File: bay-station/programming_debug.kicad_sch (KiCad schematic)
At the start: 11 parts, among them J3 USB_C_Receptacle_USB2.0_14P, SW1 BOOT, SW2 RESET

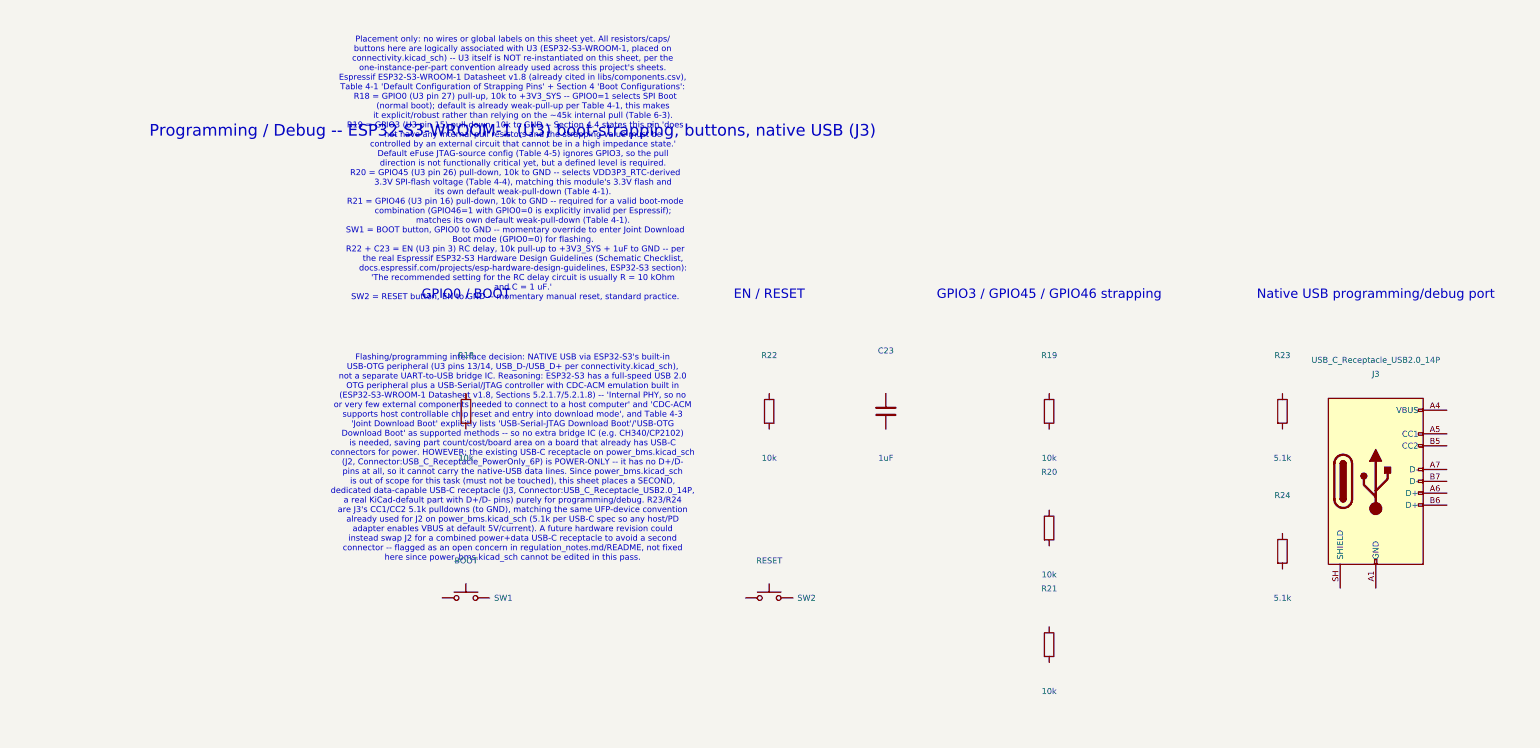
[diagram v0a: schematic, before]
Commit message: Bay station: discrete DW3210 array on a shared clock, Nordic BT840 host
Two coupled changes, both forced by the positioning scheme.

UWB ARRAY. TDoA compares timestamps across receivers, so they must share a
time base. The DWM3000 module makes that impossible -- its 24 pins contain
no clock pin and its crystal is internal and unreachable, so four of them
cannot be synchronised at any price. The bare DW3000 IC can: Datasheet v1.3
Table 10 states a 38.4 MHz signal may be supplied from an external reference
via the XTI overdrive pin. Four DW3210s (QFN40, not the 52-ball WLCSP
DW3110 the module is built on) now sit on one PCB sharing one TCXO through
a 1:4 low-skew buffer, with the antennas remote on ~1-2 m SMA coax. This
makes synchronisation structurally absent rather than solved.

uwb_anchors.kicad_sch renamed to uwb_array.kicad_sch -- the four receivers
are one on-board array, not distributed anchor units. U4 is A0, the CENTER
anchor; U5-U7 are A1-A3 outer. They are not interchangeable peers.

New clock_dist.kicad_sch holds the shared reference network. Placed are only
the passives the datasheet actually specifies: 2200 pF AC coupling into each
XTI and 1 pF from each XTO to ground, both required only because an external
clock is used. TCXO and buffer parts are not yet selected.

HOST MCU. The uplink moved from WiFi-to-internet to BLE-to-a-laptop, and
WiFi was the only thing keeping this board off Nordic. ESP32-S3-WROOM-1 is
replaced by a Fanstel BT840 (nRF52840), which gives one toolchain across
both boards and aligns with Qorvo's DW3000 reference stack -- easing the
multi-instance driver work that sits on the critical path. Note the
ESP32-S3 is BLE-only with no Classic/SPP, so the laptop link is a GATT
service.

programming_debug collapsed accordingly: Nordic programs over SWD, so the
boot straps, EN RC delay, BOOT button and the data-capable USB-C are gone,
replaced by a 2x5 ARM Cortex Debug header. That RESOLVES the long-standing
two-USB-C open item by deletion -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
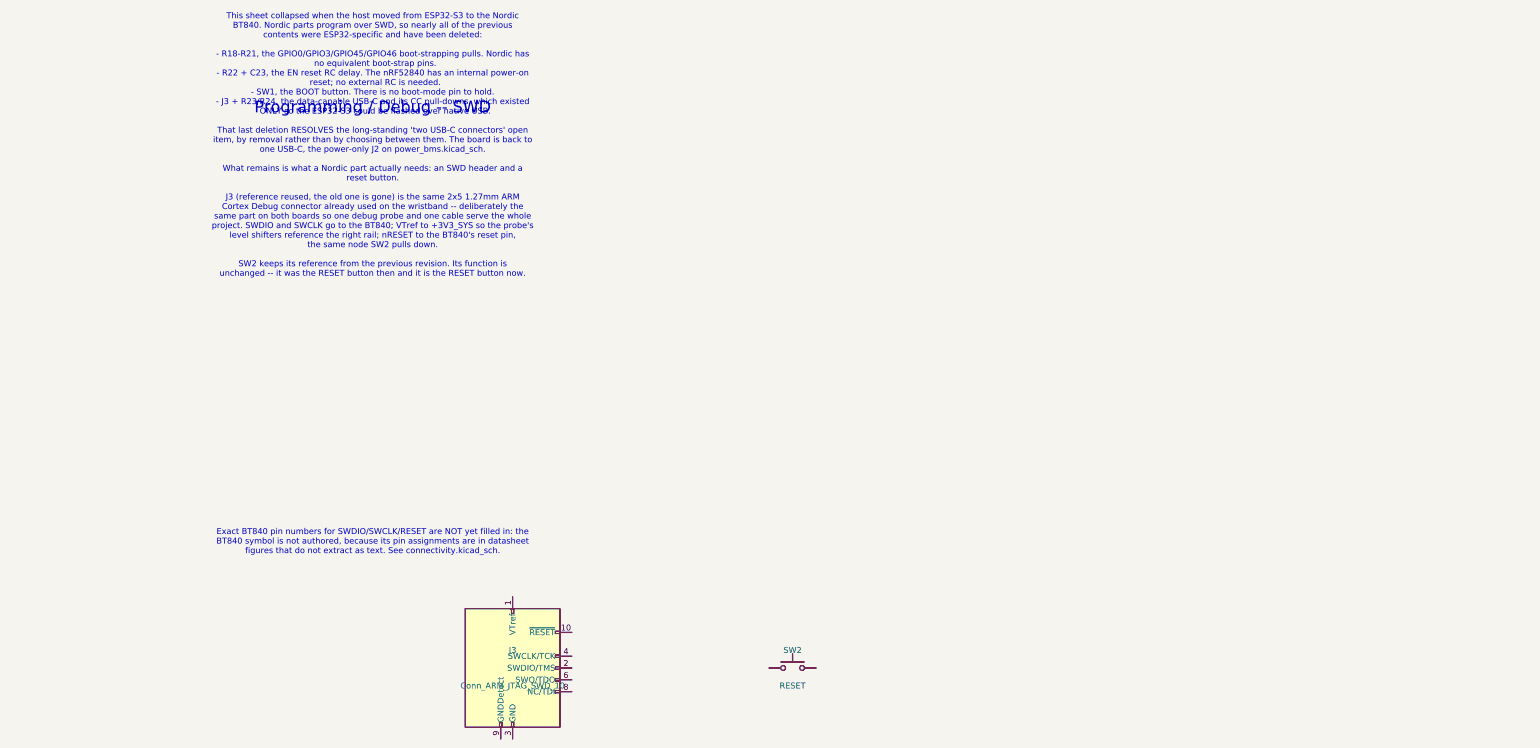
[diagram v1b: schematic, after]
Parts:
- removed C23: 1uF, Capacitor_SMD:C_0603_1608Metric, symbol Device:C
- removed J3: USB_C_Receptacle_USB2.0_14P, Connector_USB:USB_C_Receptacle_GCT_USB4105-xx-A_16P_TopMnt_Horizontal, symbol Connector:USB_C_Receptacle_USB2.0_14P
- removed R18, R19, R20, R21, R22: 10k, Resistor_SMD:R_0603_1608Metric, symbol Device:R
- removed R23, R24: 5.1k, Resistor_SMD:R_0603_1608Metric, symbol Device:R
- removed SW1: BOOT, symbol Switch:SW_Push
- added J3: Conn_ARM_JTAG_SWD_10, Connector_PinHeader_1.27mm:PinHeader_2x05_P1.27mm_Vertical, symbol Connector:Conn_ARM_JTAG_SWD_10
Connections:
- new net: J3.3 (GND), J3.5 (GND)
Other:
- note added: "Exact BT840 pin numbers for SWDIO/SWCLK/RESET are NOT yet filled in: the BT840 symbol is not authored, because its pin assignments are in datasheet figures that do not extract as text. See connectivity.kicad_sch."
- note added: "Programming / Debug -- SWD"
- note added: "This sheet collapsed when the host moved from ESP32-S3 to the Nordic BT840. Nordic parts program over SWD, so nearly all of the previous contents were ESP32-specific and have been deleted: - R18-R21, the GPIO0/GPIO3/GPIO45/GPIO46 boot-strapping pulls. Nordic has no equivalent boot-strap pins. - R22 + C23, the EN reset RC delay. The nRF52840 has an internal power-on reset; no external RC is needed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"
- note removed: "EN / RESET"
- note removed: "Flashing/programming interface decision: NATIVE USB via ESP32-S3's built-in USB-OTG peripheral (U3 pins 13/14, USB_D-/USB_D+ per connectivity.kicad_sch), not a separate UART-to-USB bridge IC. Reasoning: ESP32-S3 has a full-speed USB 2.0 OTG peripheral plus a USB-Serial/JTAG controller with CDC-ACM emulation built in (ESP32-S3-WROOM-1 Datasheet v1.8, Sections 5.2.1.7/5.2.1.8) -- 'Internal PHY, so 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"
- note removed: "GPIO0 / BOOT"
- note removed: "GPIO3 / GPIO45 / GPIO46 strapping"
- note removed: "Native USB programming/debug port"
- note removed: "Placement only: no wires or global labels on this sheet yet. All resistors/caps/ buttons here are logically associated with U3 (ESP32-S3-WROOM-1, placed on connectivity.kicad_sch) -- U3 itself is NOT re-instantiated on this sheet, per the one-instance-per-part convention already used across this project's sheets. Espressif ESP32-S3-WROOM-1 Datasheet v1.8 (already cited in libs/components.csv), Ta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"
- note removed: "Programming / Debug -- ESP32-S3-WROOM-1 (U3) boot-strapping, buttons, native USB (J3)"
